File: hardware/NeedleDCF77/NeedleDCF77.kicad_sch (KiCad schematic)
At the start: 76 parts, among them J1 USB_C_Receptacle_USB2.0

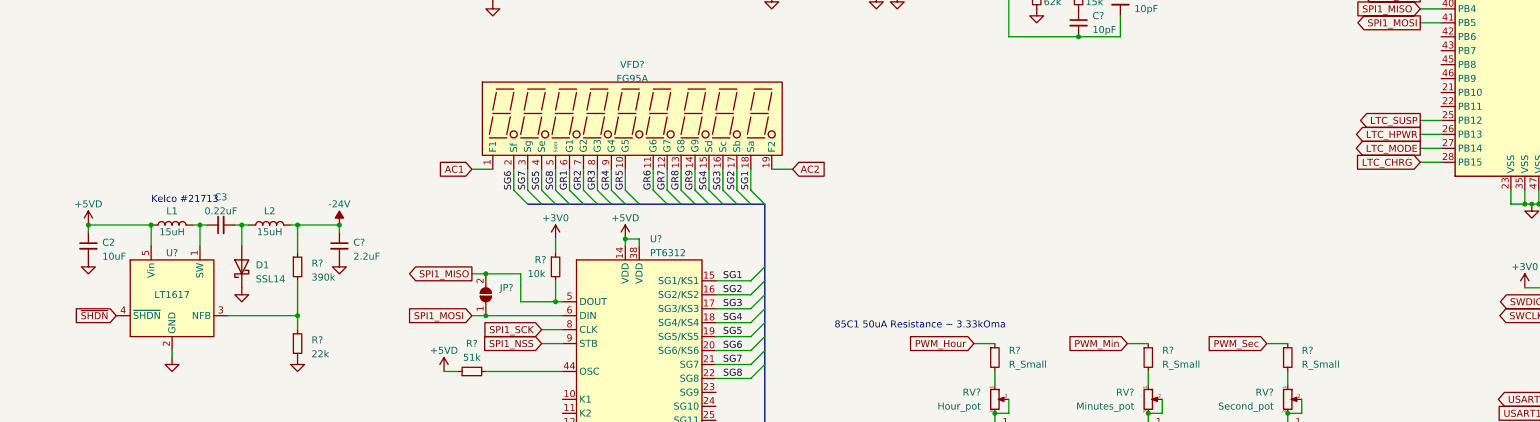
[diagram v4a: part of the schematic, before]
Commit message: Connect LT1617 shutdown to MCU
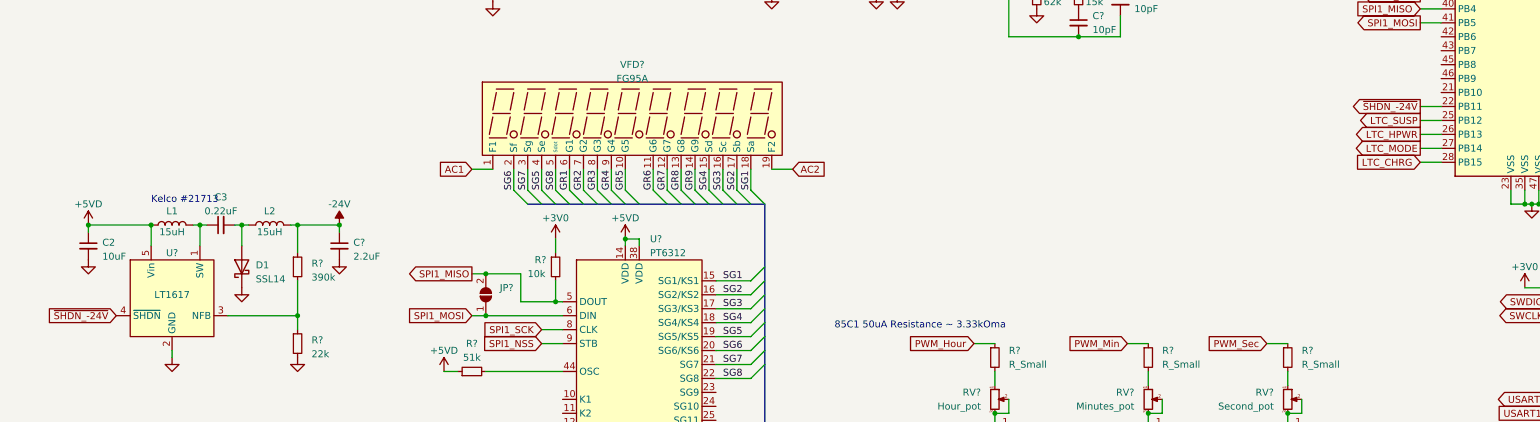
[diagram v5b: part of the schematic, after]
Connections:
- net ~{SHDN} is gone; now on net ~{SHDN_-24V}: U?.4 (~{SHDN})
- net ~{SHDN_-24V}: now reaches U?.22 (PB11)
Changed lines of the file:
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@@
+    (stroke (width 0) (type default))
+  )
+  (wire (pts (xy 265.43 95.25) (xy 269.24 95.25))
     (stroke (width 0) (type default))
   )
@@
     )
   )
-  (global_label "~{SHDN}" (shape input) (at 27.94 133.35 180) (fields_autoplaced)
-    (effects (font (size 1.27 1.27)) (justify right))
-    (property "Intersheetrefs" "${INTERSHEET_REFS}" (at 19.8937 133.35 0)
+  (global_label "~{SHDN_-24V}" (shape input) (at 27.94 133.35 180) (fields_autoplaced)
+    (effects (font (size 1.27 1.27)) (justify right))
+    (property "Intersheetrefs" "${INTERSHEET_REFS}" (at 13.8461 133.35 0)
       (effects (font (size 1.27 1.27)) (justify right) hide)
     )
@@
       (effects (font (size 1.27 1.27)) (justify right) hide)
     )
+  )
+  (global_label "~{SHDN_-24V}" (shape output) (at 265.43 95.25 180) (fields_autoplaced)
+    (effects (font (size 1.27 1.27)) (justify right))
+    (property "Intersheetrefs" "${INTERSHEET_REFS}" (at 251.3361 95.25 0)
+      (effects (font (size 1.27 1.27)) (justify right) hide)
+    )

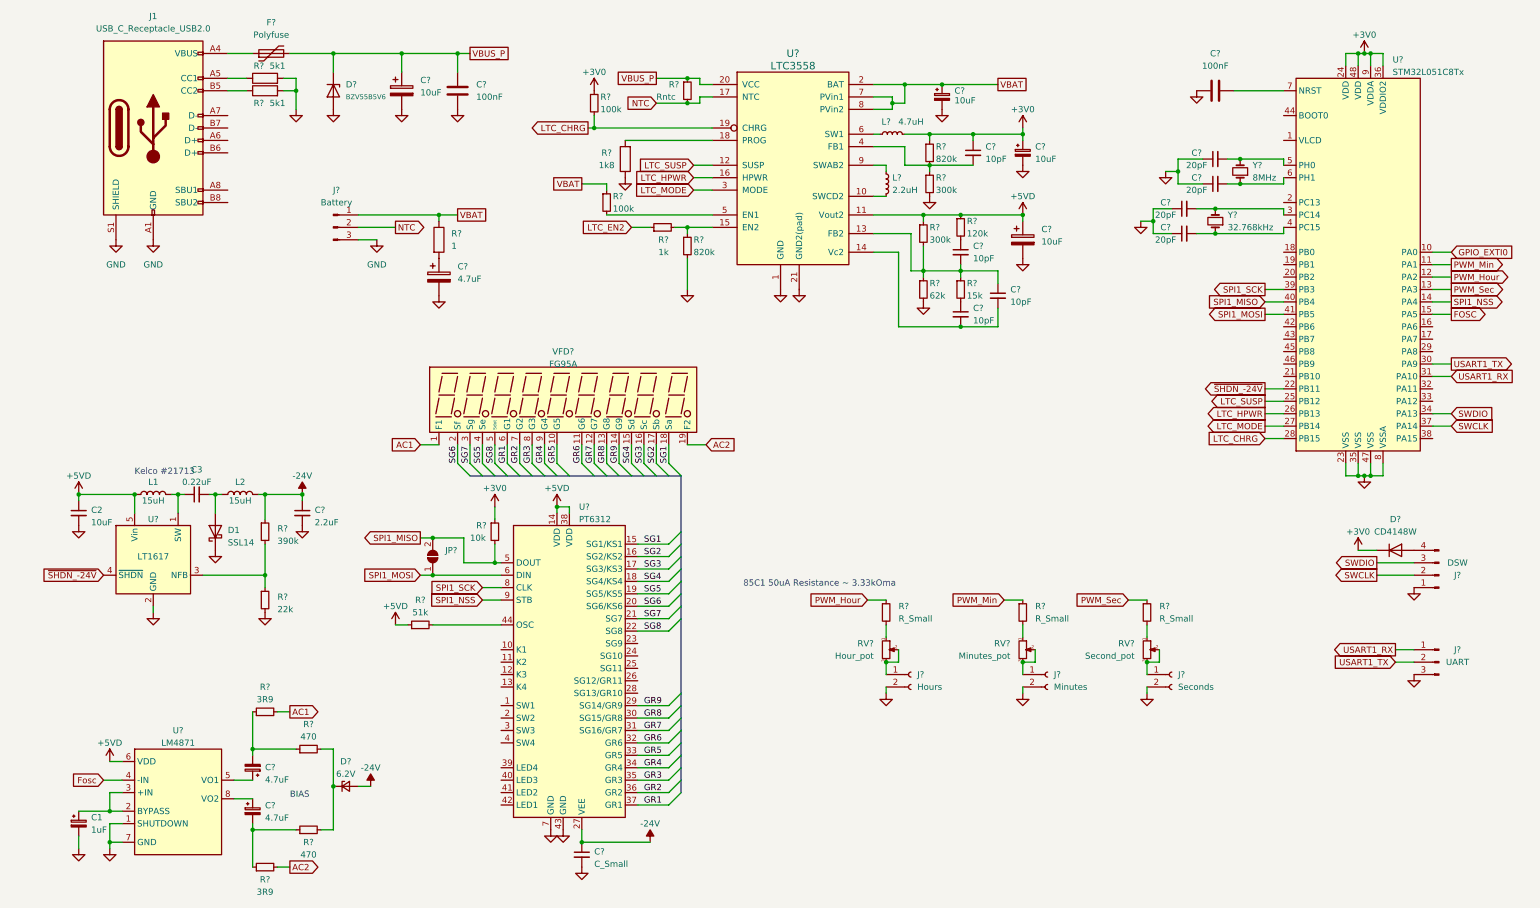
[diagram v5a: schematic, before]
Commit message: Name Fosc signal correctly
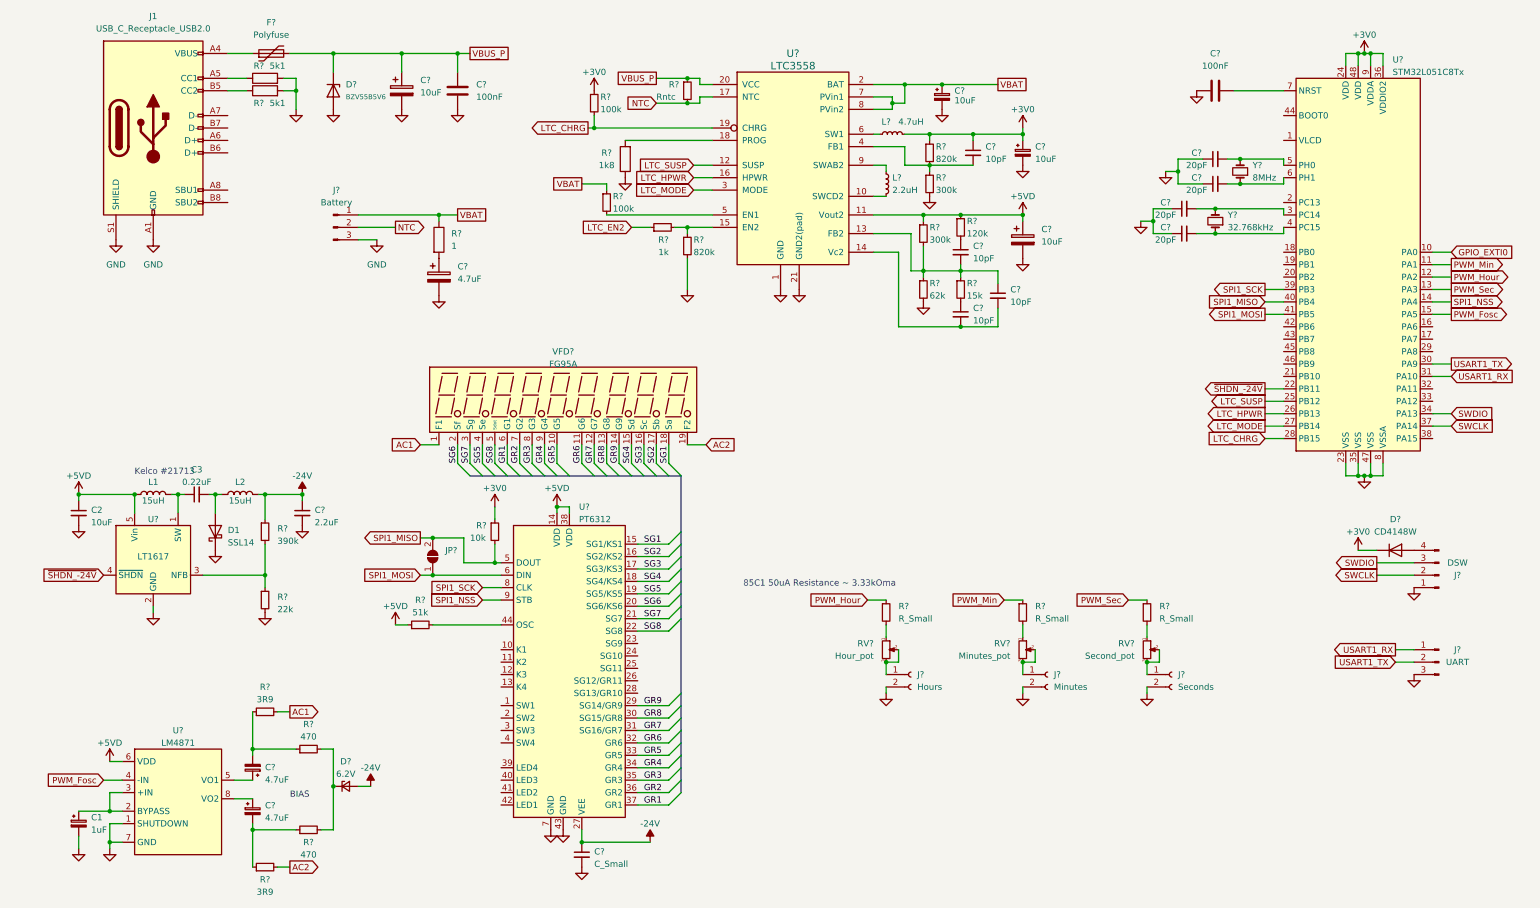
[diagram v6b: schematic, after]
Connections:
- net Fosc is gone; now on net PWM_Fosc: U?.4 (-IN)
- net FOSC renamed PWM_Fosc
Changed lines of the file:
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@@
     )
   )
-  (global_label "FOSC" (shape output) (at 303.53 80.01 0) (fields_autoplaced)
+  (global_label "PWM_Fosc" (shape output) (at 303.53 80.01 0) (fields_autoplaced)
     (effects (font (size 1.27 1.27)) (justify left))
-    (property "Intersheetrefs" "${INTERSHEET_REFS}" (at 311.3344 80.01 0)
+    (property "Intersheetrefs" "${INTERSHEET_REFS}" (at 315.9305 80.01 0)
       (effects (font (size 1.27 1.27)) (justify left) hide)
     )
@@
     )
   )
-  (global_label "Fosc" (shape input) (at 27.94 175.26 180) (fields_autoplaced)
+  (global_label "PWM_Fosc" (shape input) (at 27.94 175.26 180) (fields_autoplaced)
     (effects (font (size 1.27 1.27)) (justify right))
-    (property "Intersheetrefs" "${INTERSHEET_REFS}" (at 20.6799 175.26 0)
+    (property "Intersheetrefs" "${INTERSHEET_REFS}" (at 15.5395 175.26 0)
       (effects (font (size 1.27 1.27)) (justify right) hide)
     )

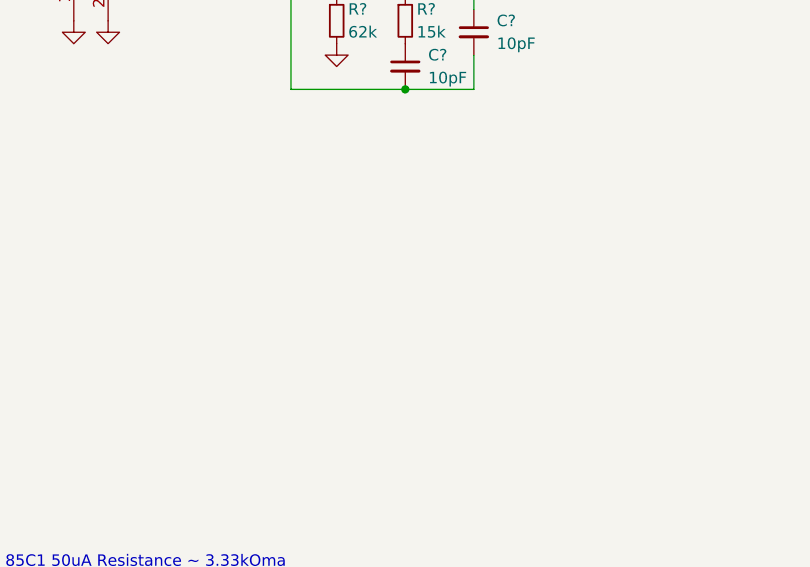
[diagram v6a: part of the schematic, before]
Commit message: Add DCF77 receiver module
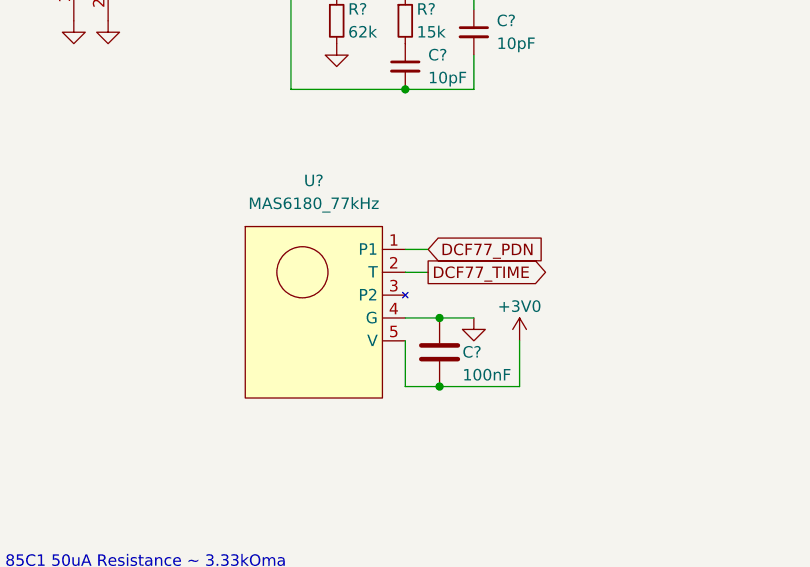
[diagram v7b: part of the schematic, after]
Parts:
- added C?: 100nF, symbol Device:C
- added U?: MAS6180_77kHz, DCF77_module:MAS6180_module, symbol DCF77Module:MAS6180_77kHz
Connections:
- net +3V0: now also C?.2, U?.5 (V)
- net GND: now also C?.1, U?.4 (G)
- new net DCF77_PDN: U?.1 (P1)
- new net DCF77_TIME: U?.2 (T)
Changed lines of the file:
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@@
   (junction (at 215.9 151.13) (diameter 0) (color 0 0 0 0)
   )
+  (junction (at 207.01 107.95) (diameter 0) (color 0 0 0 0)
+  )
   (junction (at 195.58 59.69) (diameter 0) (color 0 0 0 0)
   )
@@
   (junction (at 196.85 43.18) (diameter 0) (color 0 0 0 0)
   )
+  (junction (at 207.01 115.57) (diameter 0) (color 0 0 0 0)
+  )
   (junction (at 203.2 82.55) (diameter 0) (color 0 0 0 0)
   )
@@
     (stroke (width 0) (type default))
   )
+  (wire (pts (xy 215.9 110.49) (xy 215.9 115.57))
+    (stroke (width 0) (type default))
+  )
   (wire (pts (xy 191.77 49.53) (xy 196.85 49.53))
     (stroke (width 0) (type default))
@@
     (stroke (width 0) (type default))
   )
+  (wire (pts (xy 203.2 115.57) (xy 207.01 115.57))
+    (stroke (width 0) (type default))
+  )
   (wire (pts (xy 92.71 125.73) (xy 95.25 125.73))
     (stroke (width 0) (type default))
@@
     (stroke (width 0) (type default))
   )
+  (wire (pts (xy 203.2 102.87) (xy 205.74 102.87))
+    (stroke (width 0) (type default))
+  )
   (wire (pts (xy 64.77 34.29) (xy 67.31 34.29))
     (stroke (width 0) (type default))
@@
     (stroke (width 0) (type default))
   )
+  (wire (pts (xy 207.01 115.57) (xy 215.9 115.57))
+    (stroke (width 0) (type default))
+  )
   (wire (pts (xy 74.93 176.53) (xy 74.93 185.42))
     (stroke (width 0) (type default))
@@
     (stroke (width 0) (type default))
   )
+  (wire (pts (xy 207.01 107.95) (xy 210.82 107.95))
+    (stroke (width 0) (type default))
+  )
   (wire (pts (xy 29.21 187.96) (xy 29.21 189.23))
     (stroke (width 0) (type default))
@@
     (stroke (width 0) (type default))
   )
+  (wire (pts (xy 203.2 110.49) (xy 203.2 115.57))
+    (stroke (width 0) (type default))
+  )
   (wire (pts (xy 284.48 26.67) (xy 284.48 29.21))
     (stroke (width 0) (type default))
@@
     (stroke (width 0) (type default))
   )
+  (wire (pts (xy 203.2 100.33) (xy 205.74 100.33))
+    (stroke (width 0) (type default))
+  )
   (wire (pts (xy 134.62 44.45) (xy 152.4 44.45))
     (stroke (width 0) (type default))
@@
     (stroke (width 0) (type default))
   )
+  (wire (pts (xy 203.2 107.95) (xy 207.01 107.95))
+    (stroke (width 0) (type default))
+  )
   (wire (pts (xy 105.41 106.68) (xy 105.41 110.49))
     (stroke (width 0) (type default))
@@
     )
   )
+  (global_label "DCF77_PDN" (shape input) (at 205.74 100.33 0) (fields_autoplaced)
+    (effects (font (size 1.27 1.27)) (justify left))
+    (property "Intersheetrefs" "${INTERSHEET_REFS}" (at 219.5315 100.33 0)
+      (effects (font (size 1.27 1.27)) (justify left) hide)
+    )
+  )
   (global_label "USART1_TX" (shape output) (at 303.53 90.17 0) (fields_autoplaced)
     (effects (font (size 1.27 1.27)) (justify left))
@@
     )
   )
+  (global_label "DCF77_TIME" (shape output) (at 205.74 102.87 0) (fields_autoplaced)
+    (effects (font (size 1.27 1.27)) (justify left))
+    (property "Intersheetrefs" "${INTERSHEET_REFS}" (at 219.8338 102.87 0)
+      (effects (font (size 1.27 1.27)) (justify left) hide)
+    )
+  )
   (global_label "LTC_EN2" (shape input) (at 135.89 62.23 180) (fields_autoplaced)
     (effects (font (size 1.27 1.27)) (justify right))
@@
     )
   )
+  (symbol (lib_id "DCF77Module:MAS6180_77kHz") (at 193.04 105.41 0) (unit 1)
+    (in_bom yes) (on_board yes) (dnp no) (fields_autoplaced)
+    (property "Reference" "U?" (at 193.04 92.71 0)
+      (effects (font (size 1.27 1.27)))
+    )
+    (property "Value" "MAS6180_77kHz" (at 193.04 95.25 0)
+      (effects (font (size 1.27 1.27)))
+    )
+    (property "Footprint" "DCF77_module:MAS6180_module" (at 193.04 105.41 0)
+      (effects (font (size 1.27 1.27)) hide)
+    )
+    (property "Datasheet" "https://elty.pl/upload/download/MAS6180/EB6180B1COB.pdf" (at 193.04 105.41 0)
+      (effects (font (size 1.27 1.27)) hide)
+    )
+    (pin "1")
+    (pin "2")
+    (pin "3")
+    (pin "4")
+    (pin "5")
+    (instances
+      (project "NeedleDCF77"
+        (path "/9538e4ed-27e6-4c37-b989-9859dc0d49e8"
+          (reference "U?") (unit 1)
+        )
+      )
+    )
+  )
   (symbol (lib_id "Connector:Conn_01x03_Male") (at 74.93 62.23 0) (unit 1)
     (in_bom yes) (on_board yes) (dnp no) (fields_autoplaced)
@@
     )
   )
+  (symbol (lib_id "power:GND") (at 210.82 107.95 0) (unit 1)
+    (in_bom yes) (on_board yes) (dnp no) (fields_autoplaced)
+    (property "Reference" "#PWR025" (at 210.82 114.3 0)
+      (effects (font (size 1.27 1.27)) hide)
+    )
+    (property "Value" "GND" (at 210.82 113.03 0)
+      (effects (font (size 1.27 1.27)) hide)
+    )
+    (property "Footprint" "" (at 210.82 107.95 0)
+      (effects (font (size 1.27 1.27)) hide)
+    )
+    (property "Datasheet" "" (at 210.82 107.95 0)
+      (effects (font (size 1.27 1.27)) hide)
+    )
+    (pin "1")
+    (instances
+      (project "NeedleDCF77"
+        (path "/9538e4ed-27e6-4c37-b989-9859dc0d49e8"
+          (reference "#PWR025") (unit 1)
+        )
+      )
+    )
+  )
   (symbol (lib_id "power:+5VD") (at 87.63 143.51 0) (unit 1)
     (in_bom yes) (on_board yes) (dnp no) (fields_autoplaced)
@@
     )
   )
+  (symbol (lib_id "power:+3V0") (at 215.9 110.49 0) (unit 1)
+    (in_bom yes) (on_board yes) (dnp no)
+    (property "Reference" "#PWR026" (at 215.9 114.3 0)
+      (effects (font (size 1.27 1.27)) hide)
+    )
+    (property "Value" "+3V0" (at 215.9 106.68 0)
+      (effects (font (size 1.27 1.27)))
+    )
+    (property "Footprint" "" (at 215.9 110.49 0)
+      (effects (font (size 1.27 1.27)) hide)
+    )
+    (property "Datasheet" "" (at 215.9 110.49 0)
+      (effects (font (size 1.27 1.27)) hide)
+    )
+    (pin "1")
+    (instances
+      (project "NeedleDCF77"
+        (path "/9538e4ed-27e6-4c37-b989-9859dc0d49e8"
+          (reference "#PWR026") (unit 1)
+        )
+      )
+    )
+  )
   (symbol (lib_id "VFD_Driver:LM4871") (at 43.18 177.8 0) (unit 1)
     (in_bom yes) (on_board yes) (dnp no)
@@
         )
       )
+    )
+  )
+  (symbol (lib_id "Device:C") (at 207.01 111.76 0) (unit 1)
+    (in_bom yes) (on_board yes) (dnp no)
+    (property "Reference" "C?" (at 209.55 111.76 0)
+      (effects (font (size 1.27 1.27)) (justify left))
+    )
+    (property "Value" "100nF" (at 209.55 114.3 0)
+      (effects (font (size 1.27 1.27)) (justify left))
+    )
+    (property "Footprint" "" (at 207.9752 115.57 0)
+      (effects (font (size 1.27 1.27)) hide)
+    )
+    (property "Datasheet" "~" (at 207.01 111.76 0)
+      (effects (font (size 1.27 1.27)) hide)
+    )
+    (pin "1")
+    (pin "2")
+    (instances
+      (project "NeedleDCF77"
+        (path "/9538e4ed-27e6-4c37-b989-9859dc0d49e8"
+          (reference "C?") (unit 1)
+        )
+      )

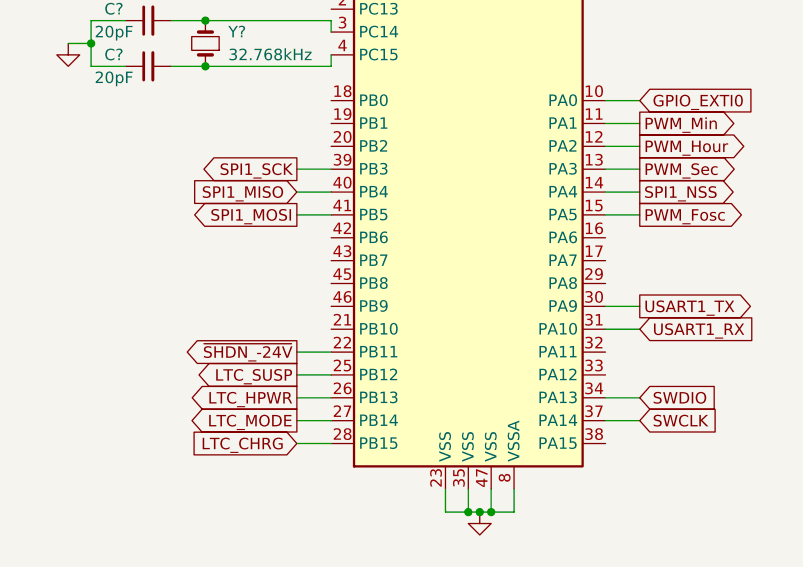
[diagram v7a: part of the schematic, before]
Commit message: Connect DCF77 module to MCU
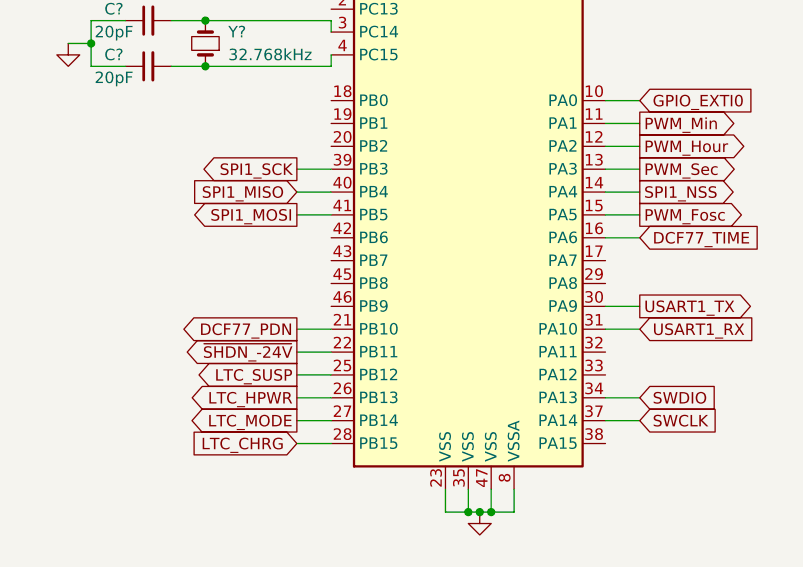
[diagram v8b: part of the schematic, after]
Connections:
- net DCF77_PDN: now also U?.21 (PB10)
- net DCF77_TIME: now also U?.16 (PA6)
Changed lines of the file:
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@@
+    (stroke (width 0) (type default))
+  )
+  (wire (pts (xy 265.43 92.71) (xy 269.24 92.71))
+    (stroke (width 0) (type default))
+  )
+  (wire (pts (xy 299.72 82.55) (xy 303.53 82.55))
     (stroke (width 0) (type default))
   )
@@
     )
   )
+  (global_label "DCF77_PDN" (shape output) (at 265.43 92.71 180) (fields_autoplaced)
+    (effects (font (size 1.27 1.27)) (justify right))
+    (property "Intersheetrefs" "${INTERSHEET_REFS}" (at 251.6385 92.71 0)
+      (effects (font (size 1.27 1.27)) (justify right) hide)
+    )
+  )
   (global_label "PWM_Min" (shape output) (at 303.53 69.85 0) (fields_autoplaced)
     (effects (font (size 1.27 1.27)) (justify left))
@@
     )
   )
+  (global_label "DCF77_TIME" (shape input) (at 303.53 82.55 0) (fields_autoplaced)
+    (effects (font (size 1.27 1.27)) (justify left))
+    (property "Intersheetrefs" "${INTERSHEET_REFS}" (at 317.6238 82.55 0)
+      (effects (font (size 1.27 1.27)) (justify left) hide)
+    )
+  )
